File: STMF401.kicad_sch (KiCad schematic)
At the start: 18 parts, among them J6 Conn_01x04_Pin, Y1 X322525MQB4SI

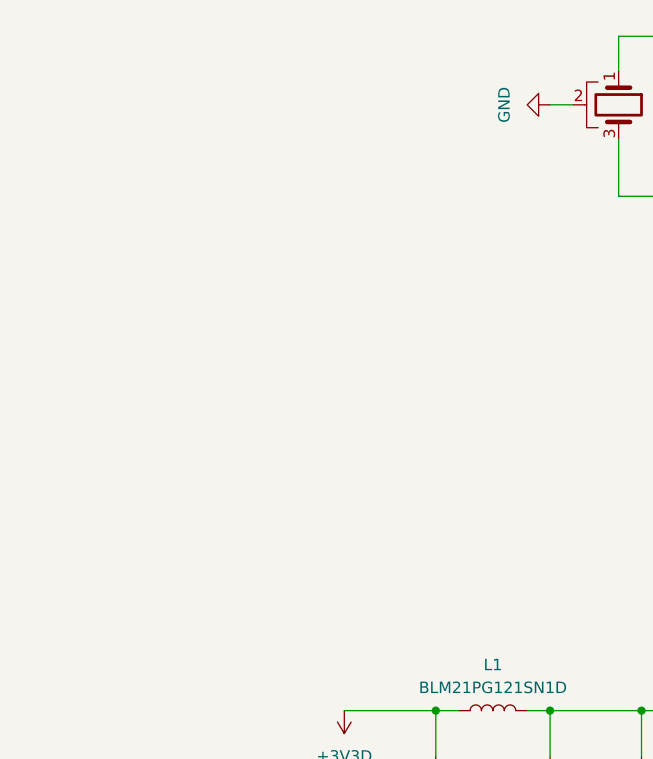
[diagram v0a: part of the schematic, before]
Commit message: feat: добавлен вход питания, кроме dc-dc
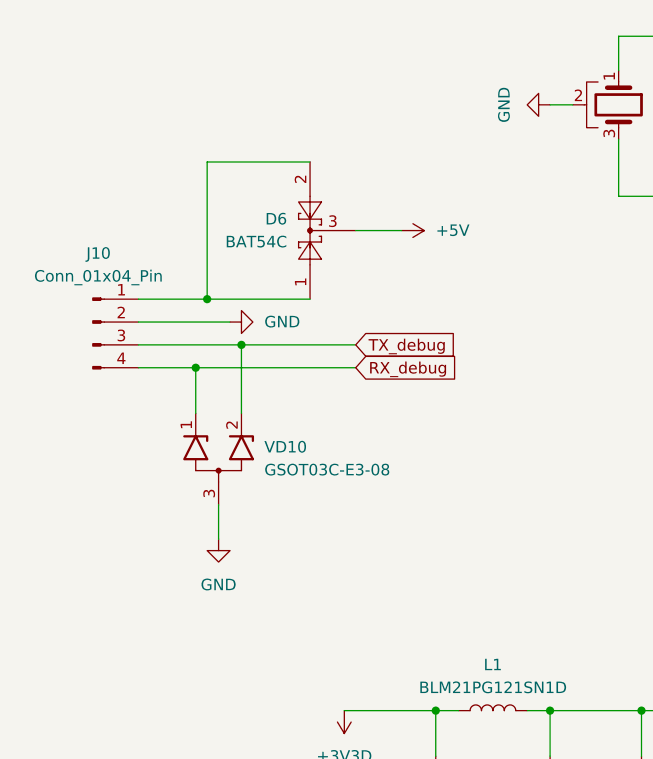
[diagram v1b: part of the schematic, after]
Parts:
- added D6: BAT54C, Package_TO_SOT_SMD:SOT-23_Handsoldering, symbol Diode:BAT54C
- added J10: Conn_01x04_Pin, Connector_PinSocket_2.54mm:PinSocket_1x04_P2.54mm_Vertical, symbol Connector:Conn_01x04_Pin
- added VD10: GSOT03C-E3-08, Package_TO_SOT_SMD:SOT-23_Handsoldering, symbol TWS:GSOT03C-E3-08
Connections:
- net GND: now also J10.2 (Pin_2), VD10.3 (A)
- net RX_debug: now also J10.4 (Pin_4), VD10.1 (K1)
- net TX_debug: now also J10.3 (Pin_3), VD10.2 (K2)
- new net: D6.1, D6.2, J10.1 (Pin_1)
- new net +5V: D6.3

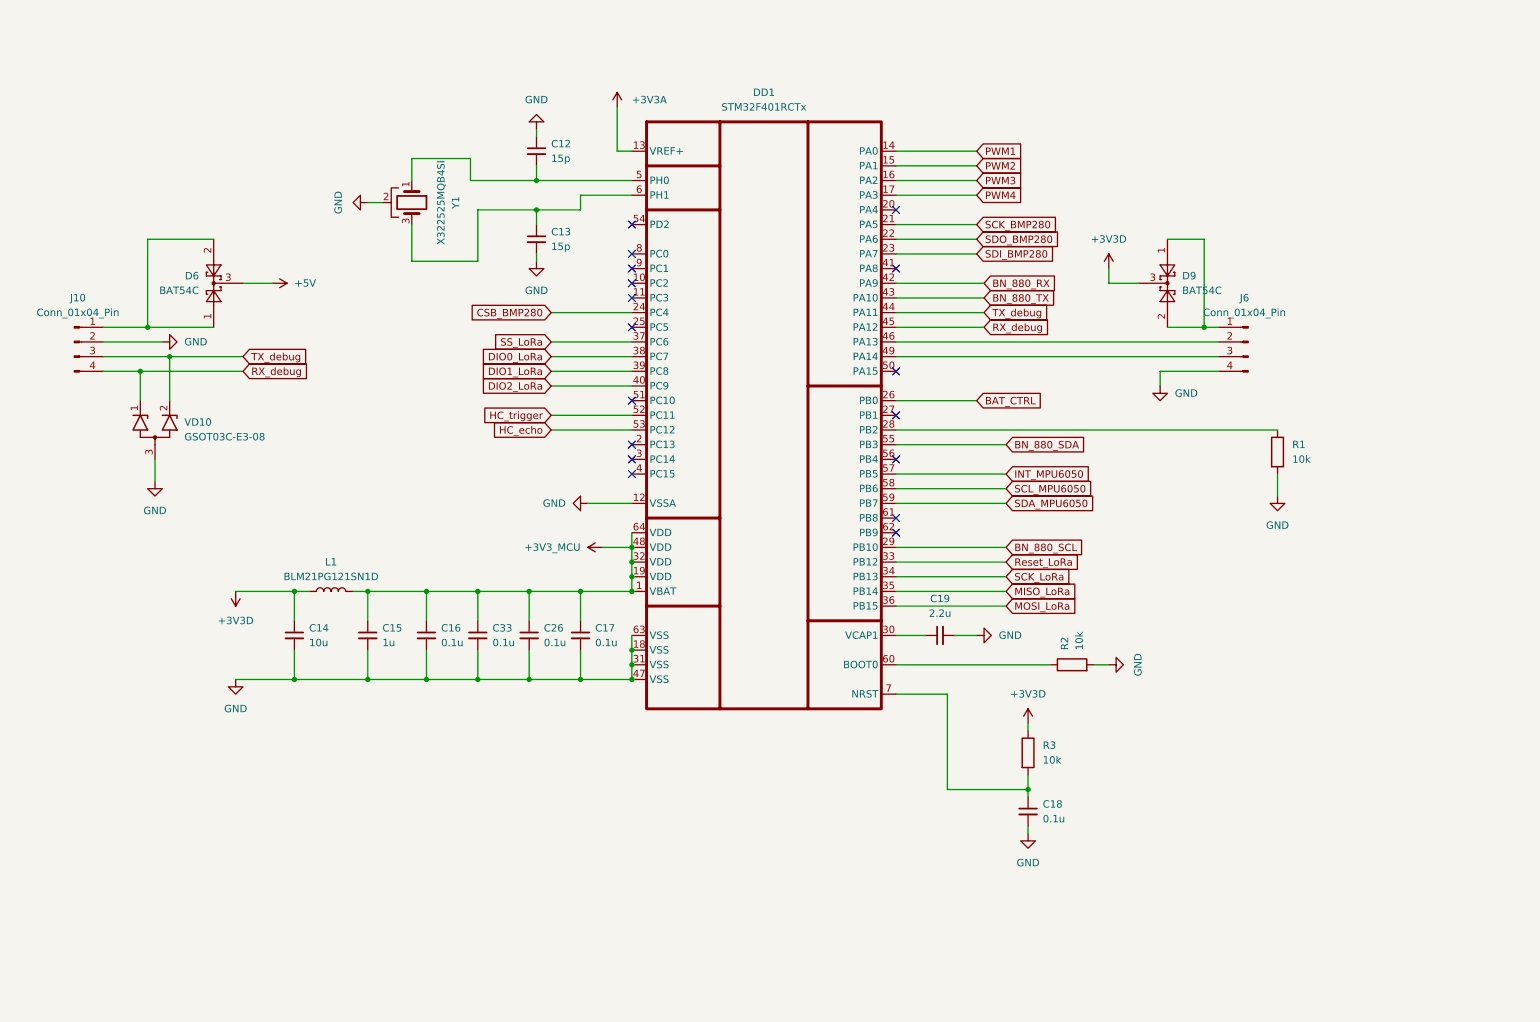
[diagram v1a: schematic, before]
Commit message: feat: доработана схема питания, расчечены габариты печатной платы
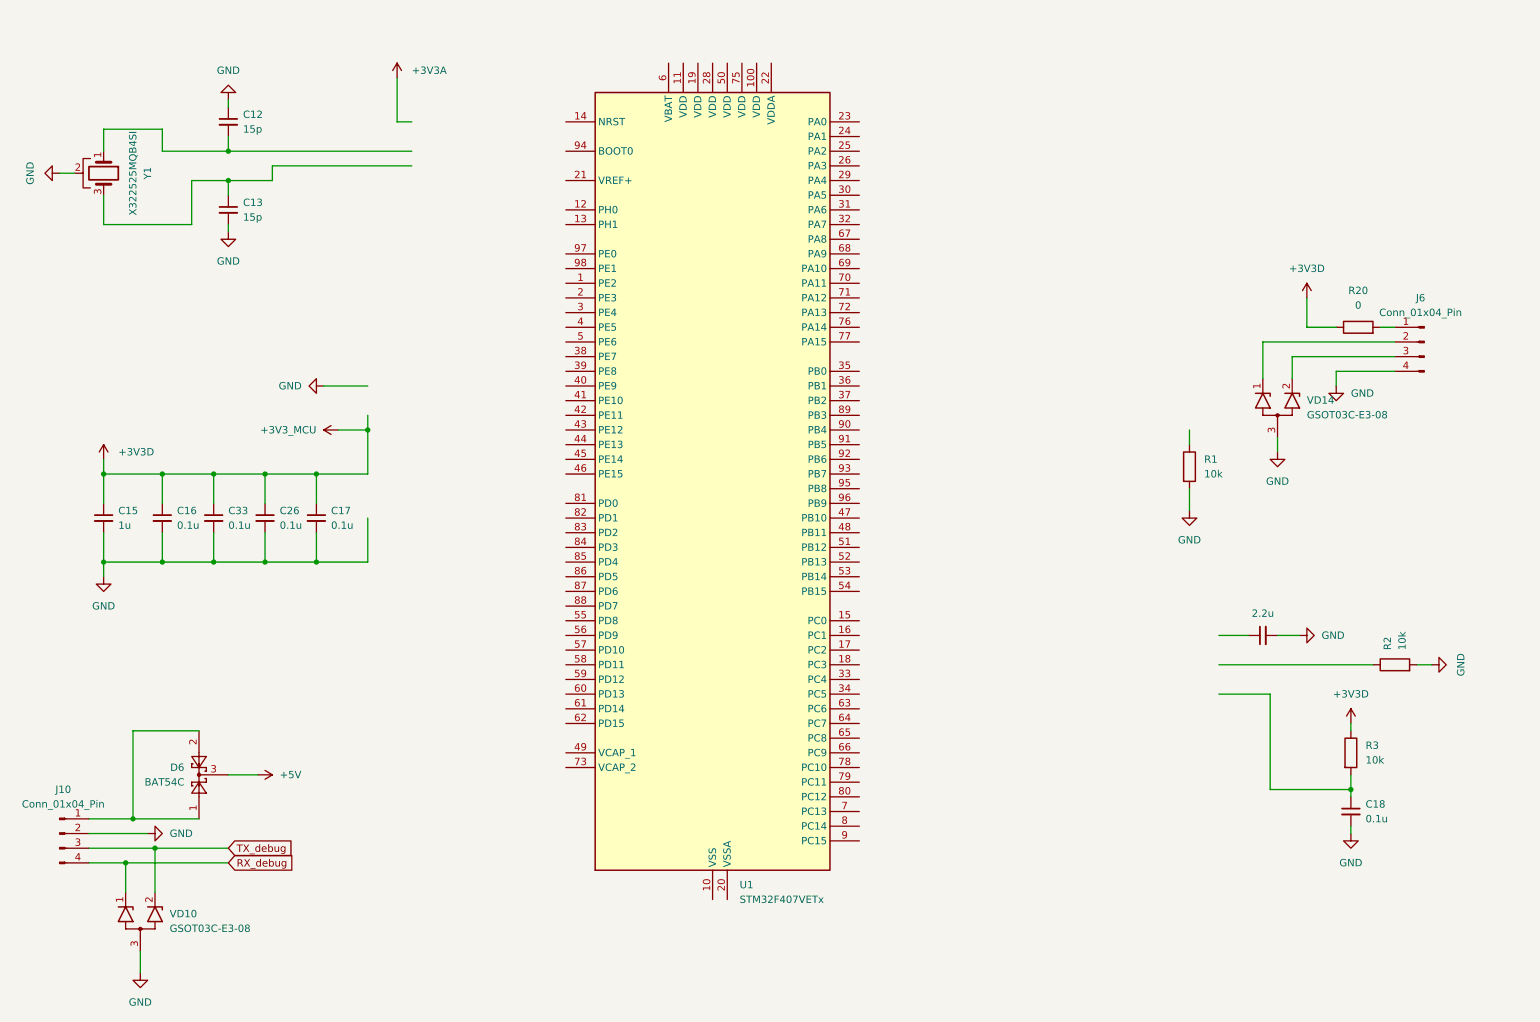
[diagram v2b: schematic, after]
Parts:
- removed C14: 10u, Capacitor_SMD:C_0805_2012Metric_Pad1.18x1.45mm_HandSolder, symbol Device:C_Small
- removed D9: BAT54C, Package_TO_SOT_SMD:SOT-23_Handsoldering, symbol Diode:BAT54C
- removed DD1: STM32F401RCTx, Package_QFP:LQFP-64_10x10mm_P0.5mm, symbol STM_MCU:STM32F401RCTx
- removed L1: BLM21PG121SN1D, Inductor_SMD:L_0805_2012Metric_Pad1.05x1.20mm_HandSolder, symbol Inductors:L
- added R20: 0, Resistor_SMD:R_0805_2012Metric_Pad1.20x1.40mm_HandSolder, symbol Device:R
- added U1: STM32F407VETx, Package_QFP:LQFP-100_14x14mm_P0.5mm, symbol MCU_ST_STM32F4:STM32F407VETx
- added VD14: GSOT03C-E3-08, Package_TO_SOT_SMD:SOT-23_Handsoldering, symbol TWS:GSOT03C-E3-08
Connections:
- net +3V3_MCU is gone; now on net +3V3D: C15.1, C16.1, C17.1, C26.1, C33.1
- net +3V3D: now also R20.1
- net GND: now also VD14.3 (A)
- net at J6.1 (Pin_1): now also R20.2
- net at J6.2 (Pin_2): now also VD14.1 (K1)
- net at J6.3 (Pin_3): now also VD14.2 (K2)
- new net: U1.10 (VSS), U1.27 (VSS), U1.74 (VSS), U1.99 (VSS)
- no-connect marks 17 -> 0
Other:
- moved on the sheet: C12, C13, C15, C16, C17, C18, C26, C33, D6, J10, J6, R1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

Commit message: feat: Добавил внешние интерфейсы
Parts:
- removed D6: BAT54C, Package_TO_SOT_SMD:SOT-23_Handsoldering, symbol Diode:BAT54C
- removed J10: Conn_01x04_Pin, Connector_PinSocket_2.54mm:PinSocket_1x04_P2.54mm_Vertical, symbol Connector:Conn_01x04_Pin
- removed U1: STM32F407VETx, Package_QFP:LQFP-100_14x14mm_P0.5mm, symbol MCU_ST_STM32F4:STM32F407VETx
- removed VD10: GSOT03C-E3-08, Package_TO_SOT_SMD:SOT-23_Handsoldering, symbol TWS:GSOT03C-E3-08
- added C31: 0.1u, Capacitor_SMD:C_0805_2012Metric_Pad1.18x1.45mm_HandSolder, symbol Device:C_Small
- added R21, R22: 3k, Resistor_SMD:R_0805_2012Metric_Pad1.20x1.40mm_HandSolder, symbol Device:R
- added U7: STM32F407VETx, Package_QFP:LQFP-100_14x14mm_P0.5mm, symbol STM_MCU:STM32F407VETx
- added U8: AT24C256, Package_SO:SOIC-8_3.9x4.9mm_P1.27mm, symbol EEPROM:AT24C256
- C15: value 1u -> 0.1u
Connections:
- net +3V3D: now also C31.1, R21.1, R22.1, U8.8 (VCC)
- net GND: now also C31.2, U8.1 (A0), U8.2 (A1), U8.3 (A2), U8.4 (GND), U8.7 (WP)
- new net EEPROM_SCL: R21.2, U8.6 (SCL)
- new net EEPROM_SDA: R22.2, U8.5 (SDA)
